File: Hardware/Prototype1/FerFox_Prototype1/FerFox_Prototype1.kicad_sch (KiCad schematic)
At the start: 23 parts, among them J1 Conn_01x08_Pin, J2 Conn_01x06_Pin, U1 STM32F401CCUx, Y1 25MHz, Y2 32768 Hz

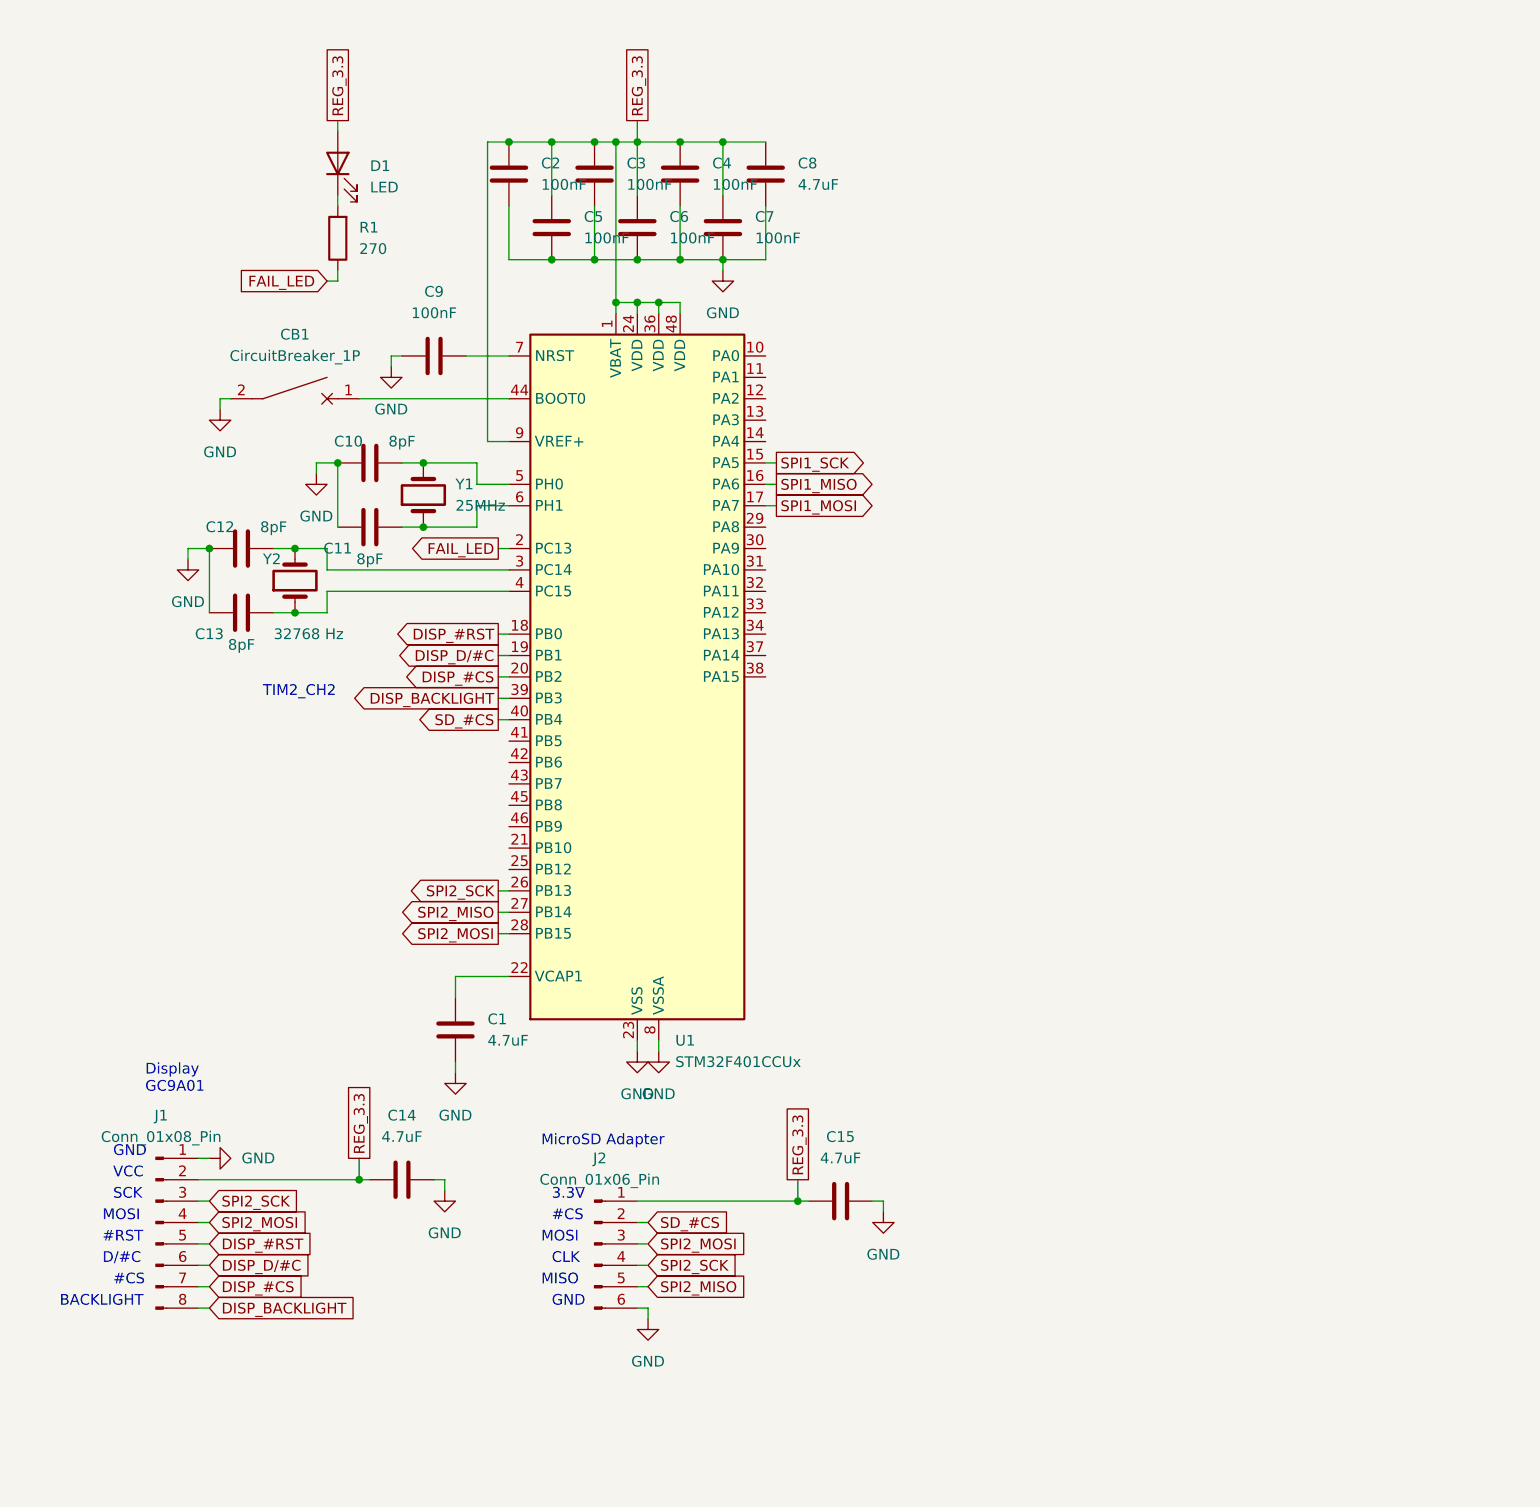
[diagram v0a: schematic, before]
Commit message: Able to initialize (kinda dirty) a SD card
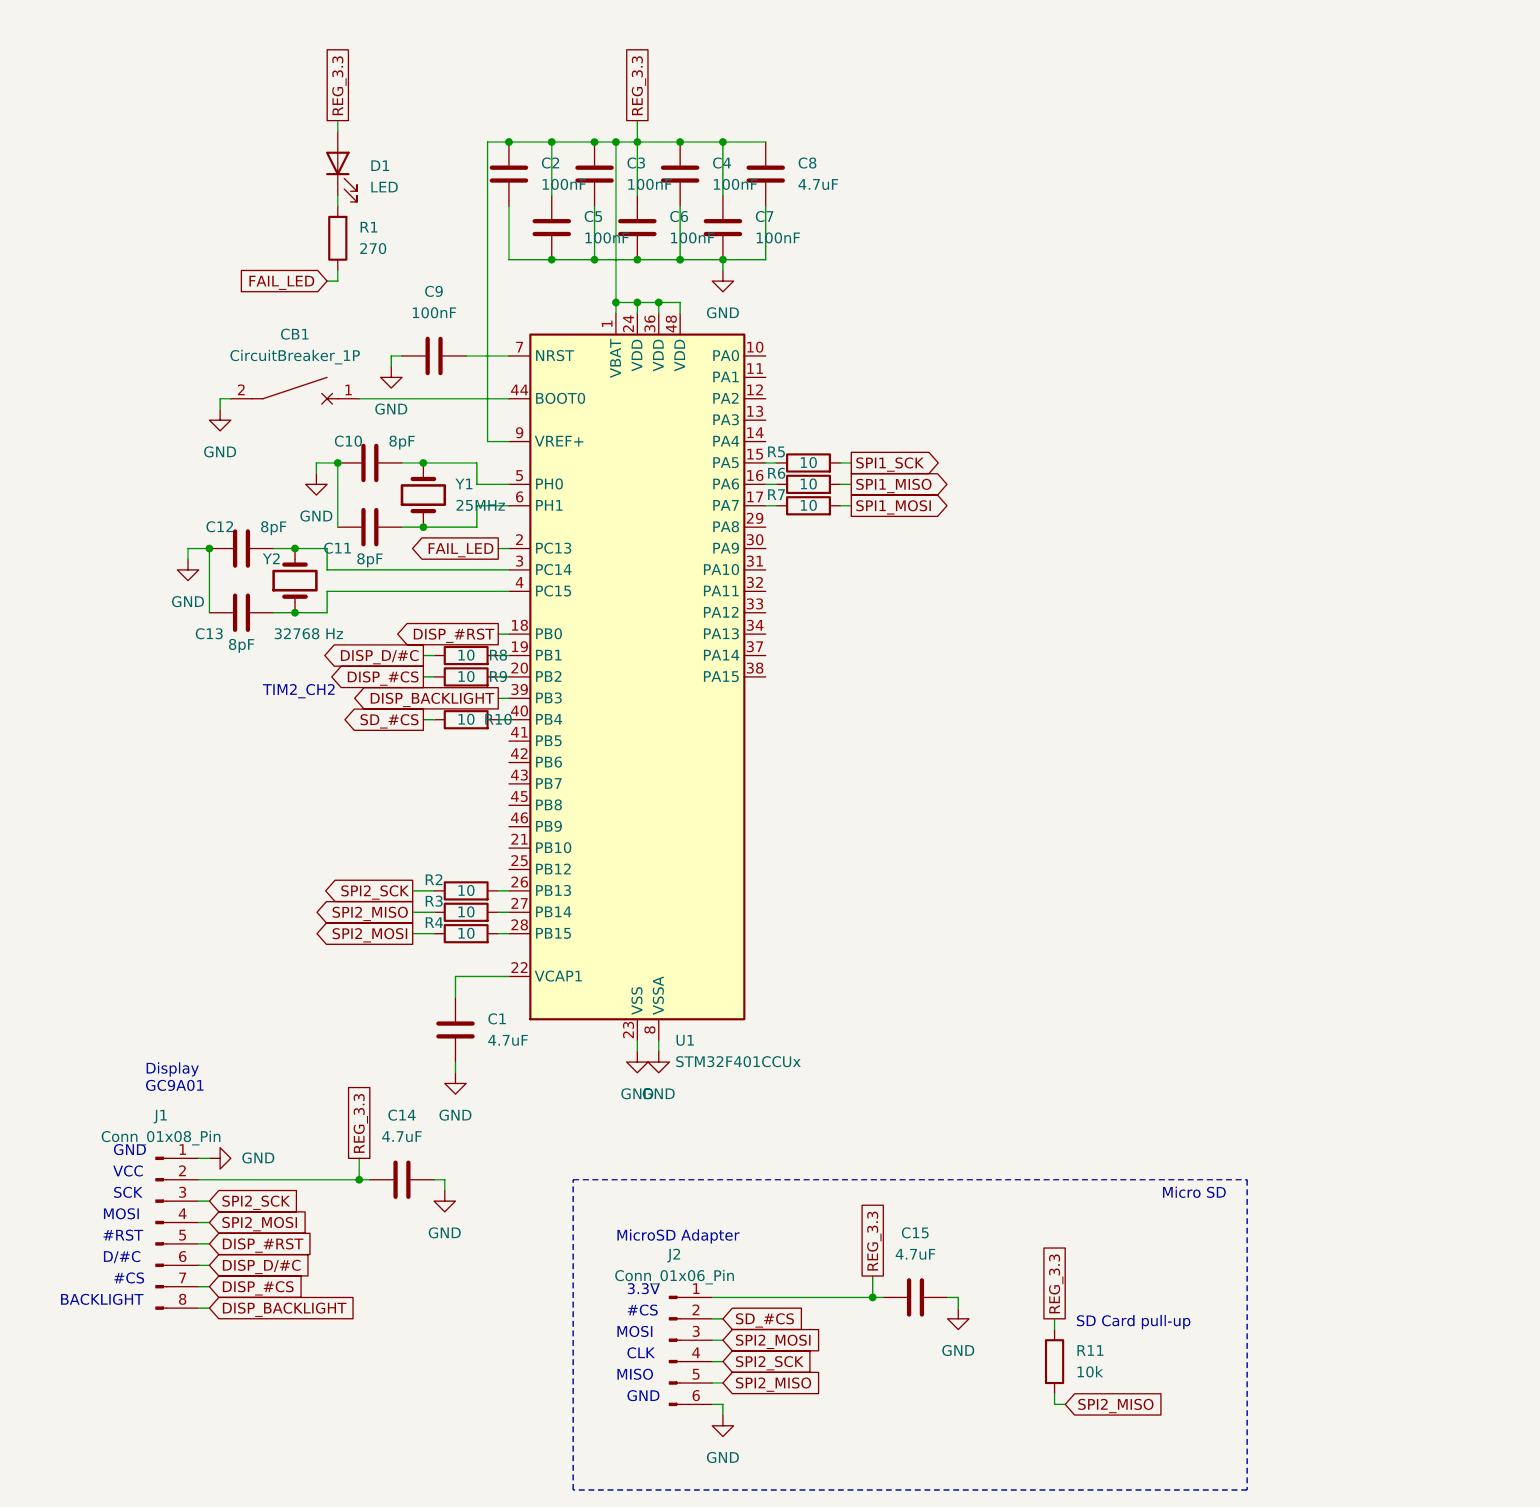
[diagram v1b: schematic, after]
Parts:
- added R10, R2, R3, R4, R5, R6, R7, R8, R9: 10, symbol Device:R
- added R11: 10k, symbol Device:R
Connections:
- net DISP_#CS: now also R9.1; no longer U1.20 (PB2)
- net DISP_D/#C: now also R8.1; no longer U1.19 (PB1)
- net REG_3.3: now also R11.1
- net SD_#CS: now also R10.1; no longer U1.40 (PB4)
- net SPI1_MISO: now also R6.2; no longer U1.16 (PA6)
- net SPI1_MOSI: now also R7.2; no longer U1.17 (PA7)
- net SPI1_SCK: now also R5.2; no longer U1.15 (PA5)
- net SPI2_MISO: now also R11.2, R3.1; no longer U1.27 (PB14)
- net SPI2_MOSI: now also R4.1; no longer U1.28 (PB15)
- net SPI2_SCK: now also R2.1; no longer U1.26 (PB13)
- new net: R9.2, U1.20 (PB2)
- new net: R10.2, U1.40 (PB4)
- new net: R4.2, U1.28 (PB15)
- new net: R7.1, U1.17 (PA7)
- new net: R5.1, U1.15 (PA5)
- new net: R6.1, U1.16 (PA6)
- new net: R8.2, U1.19 (PB1)
- new net: R2.2, U1.26 (PB13)
- new net: R3.2, U1.27 (PB14)
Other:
- note added: "Micro SD"
- note added: "SD Card pull-up"
- moved on the sheet: C15, J2

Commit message: Modifications in circuit
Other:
- note added: "Display"
- moved on the sheet: C14, J1
